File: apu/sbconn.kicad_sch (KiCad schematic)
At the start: 20 parts, among them U1 X818336-001, U2 74LVC1G04

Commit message: Internal Connectors
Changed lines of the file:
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@@
 	(bus
 		(pts
-			(xy 163.83 73.66) (xy 168.91 73.66)
+			(xy 163.83 73.66) (xy 166.37 73.66)
 		)
 		(stroke
@@
 	(bus
 		(pts
-			(xy 189.23 50.8) (xy 194.31 50.8)
+			(xy 189.23 50.8) (xy 189.23 48.26)
 		)
 		(stroke
@@
 	(bus
 		(pts
-			(xy 64.77 63.5) (xy 69.85 63.5)
+			(xy 67.31 63.5) (xy 69.85 63.5)
 		)
 		(stroke
@@
 	(hierarchical_label "{VIDEO}"
 		(shape output)
-		(at 168.91 73.66 0)
+		(at 166.37 73.66 0)
 		(effects
 			(font
@@
 	(hierarchical_label "{PCIE_X2}"
 		(shape bidirectional)
-		(at 64.77 63.5 180)
+		(at 67.31 63.5 180)
 		(effects
 			(font
@@
 	(hierarchical_label "{PCIE_X2}"
 		(shape bidirectional)
-		(at 194.31 50.8 0)
-		(effects
-			(font
+		(at 189.23 48.26 90)
+		(effects
+			(font

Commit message: Cleanup & Debug I/O
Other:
- moved on the sheet: C34, R25, R27, R28, R29, R31, R32, TP10, TP9, U2

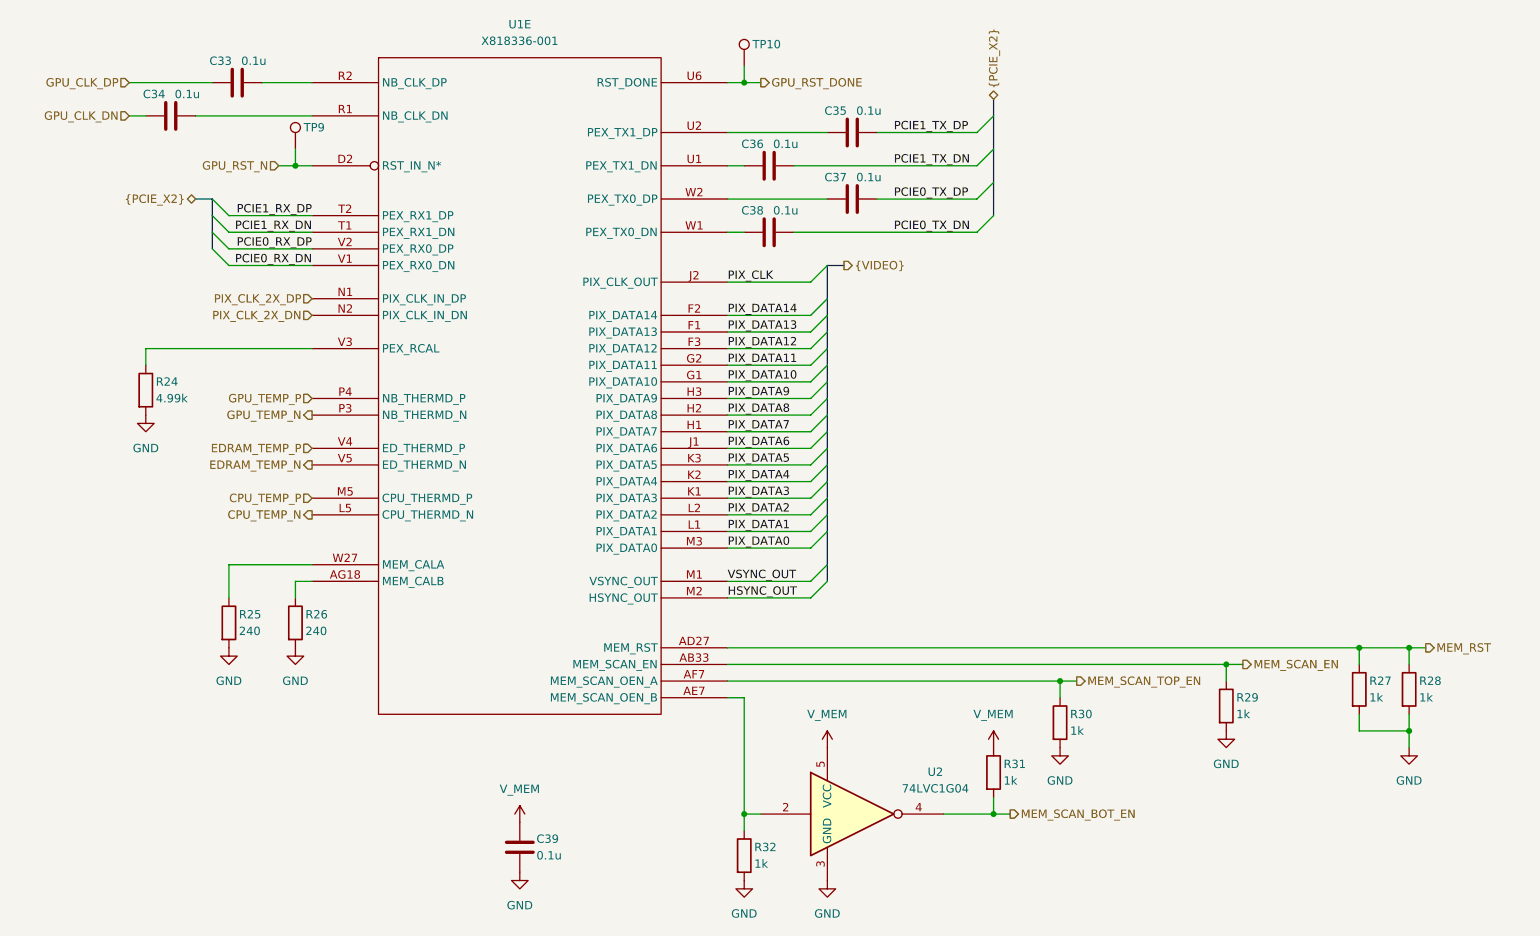
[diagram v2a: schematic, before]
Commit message: Multipurpose and standby power rails, Reannotated schematic
Added V_1P2, V_1P8, V_5P0DUAL, V_EFUSE, V_GPUPCIE, V_3P3STBY and V_1P2STBY
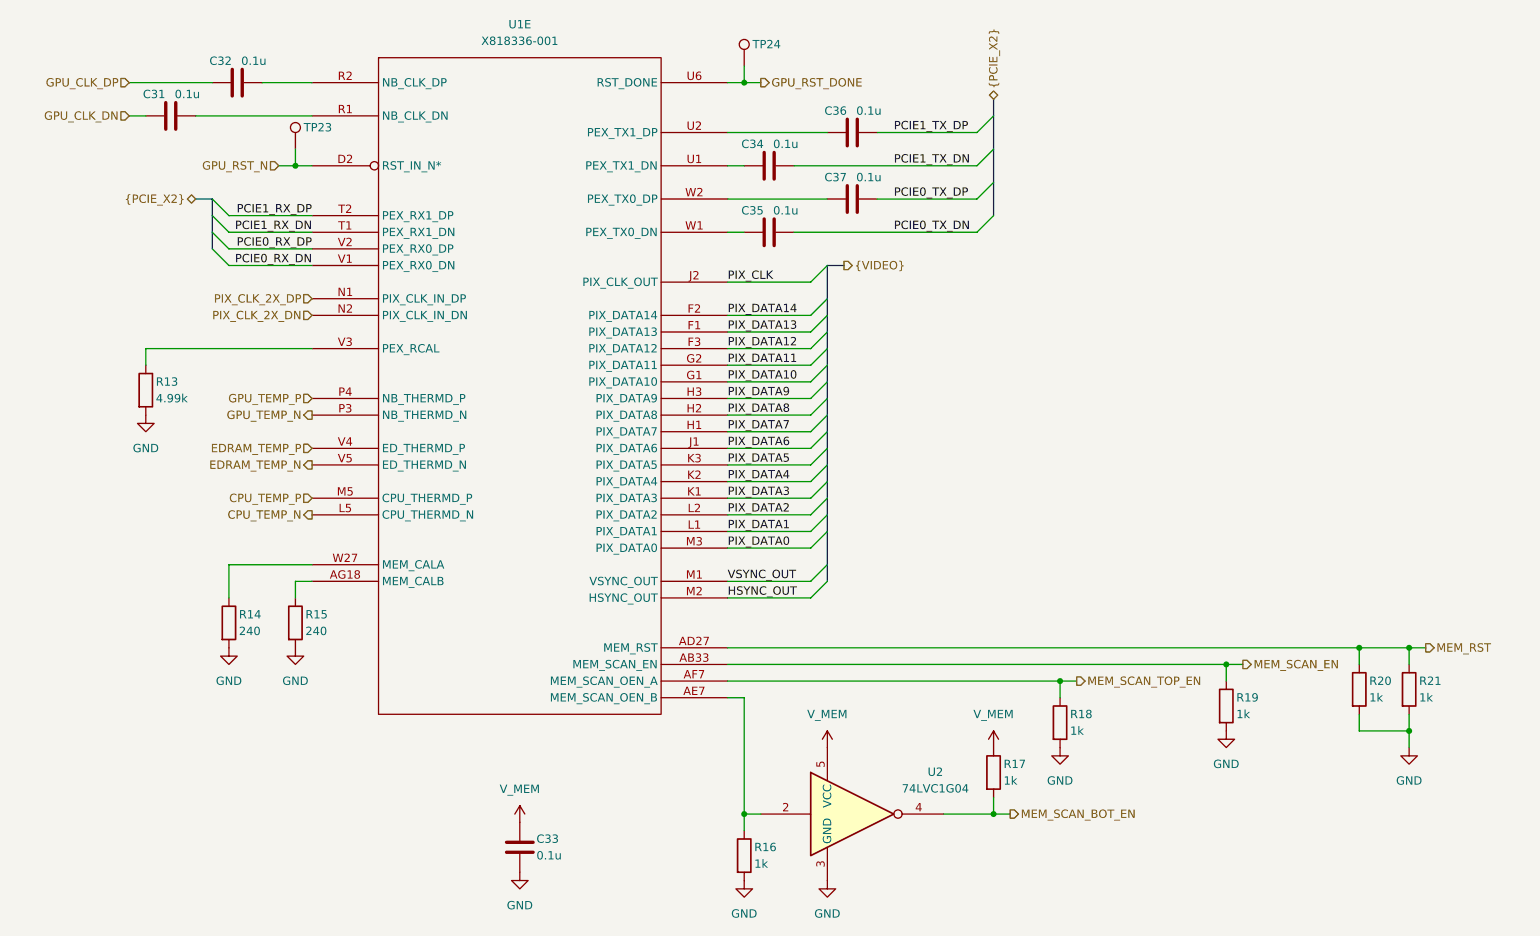
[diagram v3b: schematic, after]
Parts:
- renumbered C34 to C31, C33 to C32, C39 to C33, C36 to C34, C38 to C35, C35 to C36, R24 to R13, R25 to R14, R26 to R15, R32 to R16, R31 to R17, R30 to R18, R29 to R19, R27 to R20, R28 to R21, TP9 to TP23, TP10 to TP24
